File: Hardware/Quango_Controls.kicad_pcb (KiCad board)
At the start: 2 copper layers, 80.8 x 110 mm, 33 parts, among them J1 Conn_01x12_Male, J10 Gate_Out, J2 Conn_01x16_Male, J3 Conn_01x12_Male, J4 Conn_01x12_Male, J5 CV_A, J6 CV_B, J7 Out, J8 USB_C_Receptacle, J9 Midi_In, SW1 SW_Push, SW2 SW_Push

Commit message: Updates to Panel Graphics
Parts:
- moved J8 0.50 mm to (100.4, 124.2)
- moved J9 0.50 mm to (80.6, 124.3)
- moved R1 0.50 mm to (98.1, 124.2)
- moved R2 0.50 mm to (102.8, 124.2)
- moved TP1 0.50 mm to (91.5, 126.6)
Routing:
- net +3.3VA: track 259.7 -> 260.3 mm
- net /USB_DP: track 64.8 -> 64.2 mm

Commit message: Final Updates for v1.0 production
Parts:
- J1, J3, J4: footprint Connector_PinHeader_2.54mm:PinHeader_1x12_P2.54mm_Vertical -> Connector_PinSocket_2.54mm:PinSocket_1x12_P2.54mm_Vertical
- J2: footprint Connector_PinHeader_2.54mm:PinHeader_1x16_P2.54mm_Vertical -> Connector_PinSocket_2.54mm:PinSocket_1x16_P2.54mm_Vertical
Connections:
- J2 pad 13: /Gate3_Out -> /Gate4_Out
- J2 pad 14: /Gate4_Out -> /Gate3_Out
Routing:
- net /Gate3_Out: track 34.5 -> 31.6 mm
- net /MIDI_IN: track 100.3 -> 99.3 mm
- net +3.3VA: track 260.3 -> 259.6 mm
- net GND: vias 4 -> 84

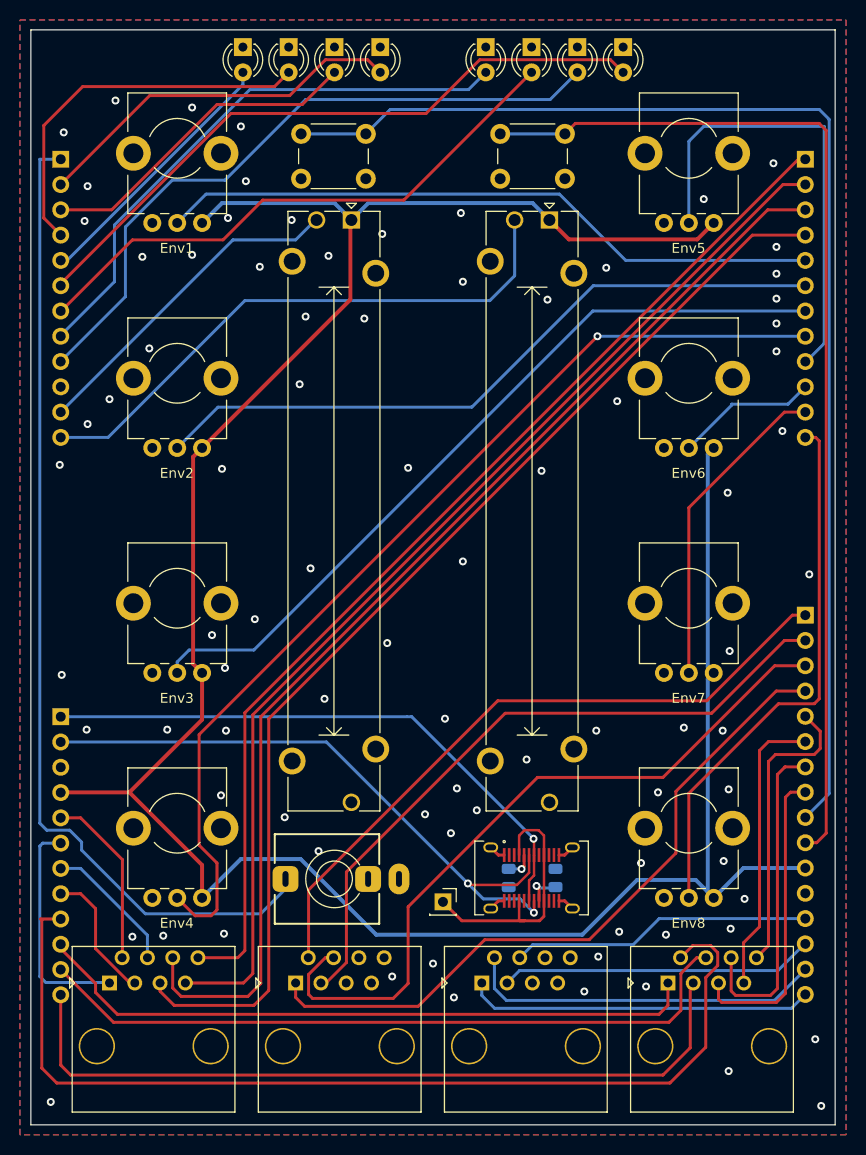
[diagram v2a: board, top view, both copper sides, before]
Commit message: Updated controls to include octave switching; revised panel
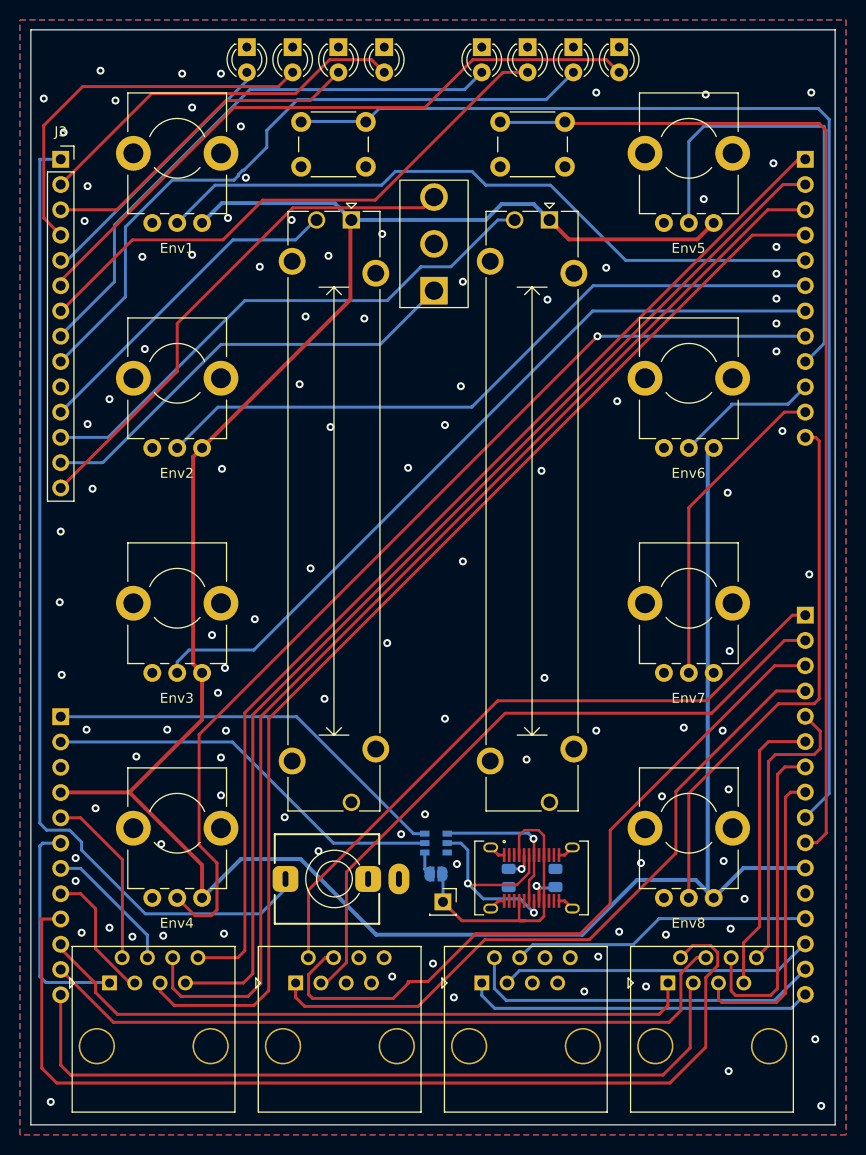
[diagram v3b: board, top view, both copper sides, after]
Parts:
- added JP1: Jumper, Jumper:SolderJumper-2_P1.3mm_Open_RoundedPad1.0x1.5mm, B.Cu at (90.8, 123.8)
- added SW3: Octave_Switch, Custom_Footprints:SP3T_Mini_Switch, F.Cu at (90.6, 60.5)
- added U1: STF202-22T1G, Custom_Footprints:STF202-22T1G, B.Cu at (90.8, 120.7)
- J3: value Conn_01x12_Male -> Conn_01x14_Male; footprint Connector_PinSocket_2.54mm:PinSocket_1x12_P2.54mm_Vertical -> Connector_PinSocket_2.54mm:PinSocket_1x14_P2.54mm_Vertical; moved to F.Cu
- moved SW1 1.20 mm to (80.5, 50.5)
- moved SW2 1.20 mm to (100.5, 50.5)
- moved A2 0.40 mm to (76.4, 42.0)
- moved A3 0.40 mm to (81.0, 42.0)
- moved B2 0.40 mm to (100.0, 42.0)
- moved B3 0.40 mm to (104.6, 42.0)
- moved A1 0.40 mm to (71.8, 42.0)
- moved A4 0.40 mm to (85.6, 42.0)
- moved B1 0.40 mm to (95.4, 42.0)
- moved B4 0.40 mm to (109.2, 42.0)
- turned J3 to 0 degrees
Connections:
- net Net-(J8-PadA4) renamed /VBUS
- J8 pad A6: /USB_DP -> /D+
- J8 pad A7: /USB_DM -> /D-
- J8 pad B6: /USB_DP -> /D+
- J8 pad B7: /USB_DM -> /D-
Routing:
- net /Octave_Down: track 0.00 -> 52.4 mm
- net /Octave_Up: track 0.00 -> 44.7 mm
- net /USB_DP: track 64.5 -> 40.8 mm, vias 2 -> 0
- net /D+: track 0.00 -> 23.4 mm, vias 0 -> 2
- net /USB_DM: track 59.0 -> 41.4 mm, vias 1 -> 0
- net /D-: track 0.00 -> 15.4 mm, vias 0 -> 1
- net /ChannelB_Level: track 57.9 -> 54.6 mm
- net /VBUS: track 26.6 -> 29.5 mm
- net Net-(JP1-Pad1): track 0.00 -> 2.35 mm
- net /Env1_Attack: track 67.1 -> 68.9 mm
- net /EnvB3_LED_Out: track 68.0 -> 68.7 mm
- net GND: vias 84 -> 104
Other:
- board text added: "Mountjoy Modular 2023 Quango Controls v2.0"
- board text removed: "Mountjoy Modular 2023 Quango Controls v1.0"

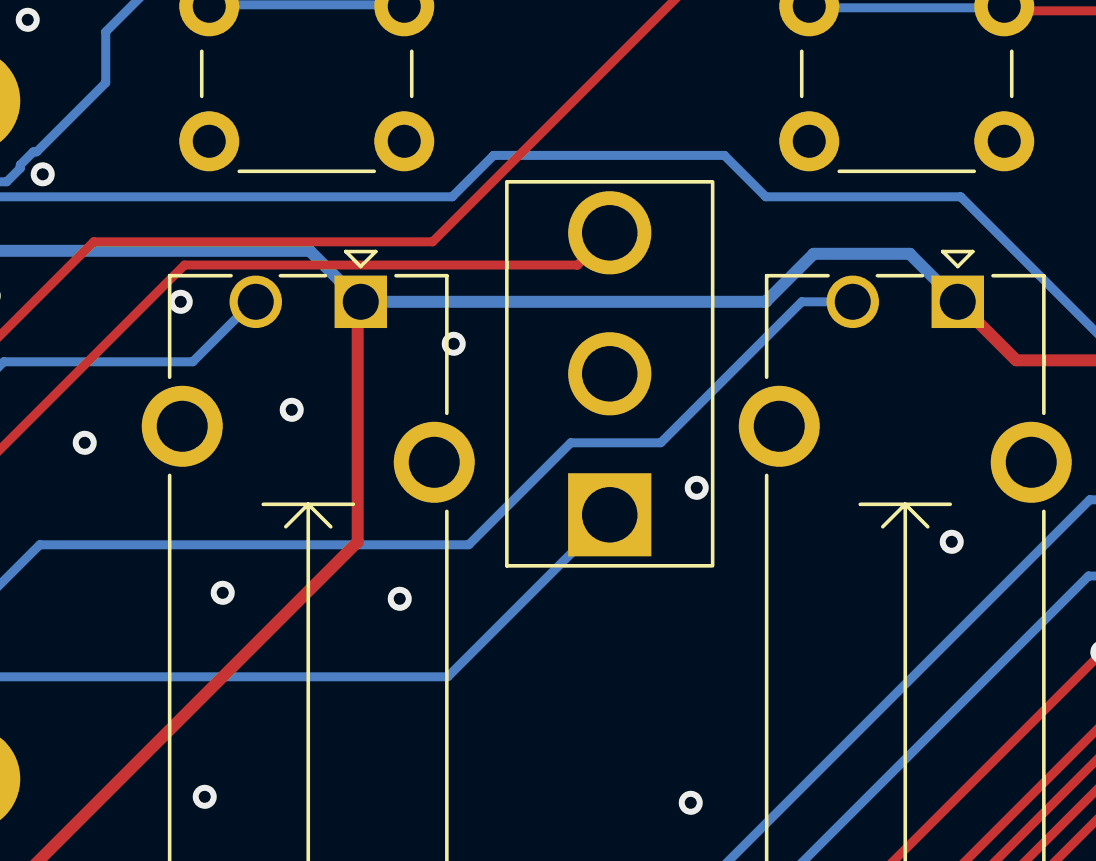
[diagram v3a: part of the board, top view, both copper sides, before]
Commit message: Prepared v2 controls and panel for  manufacture
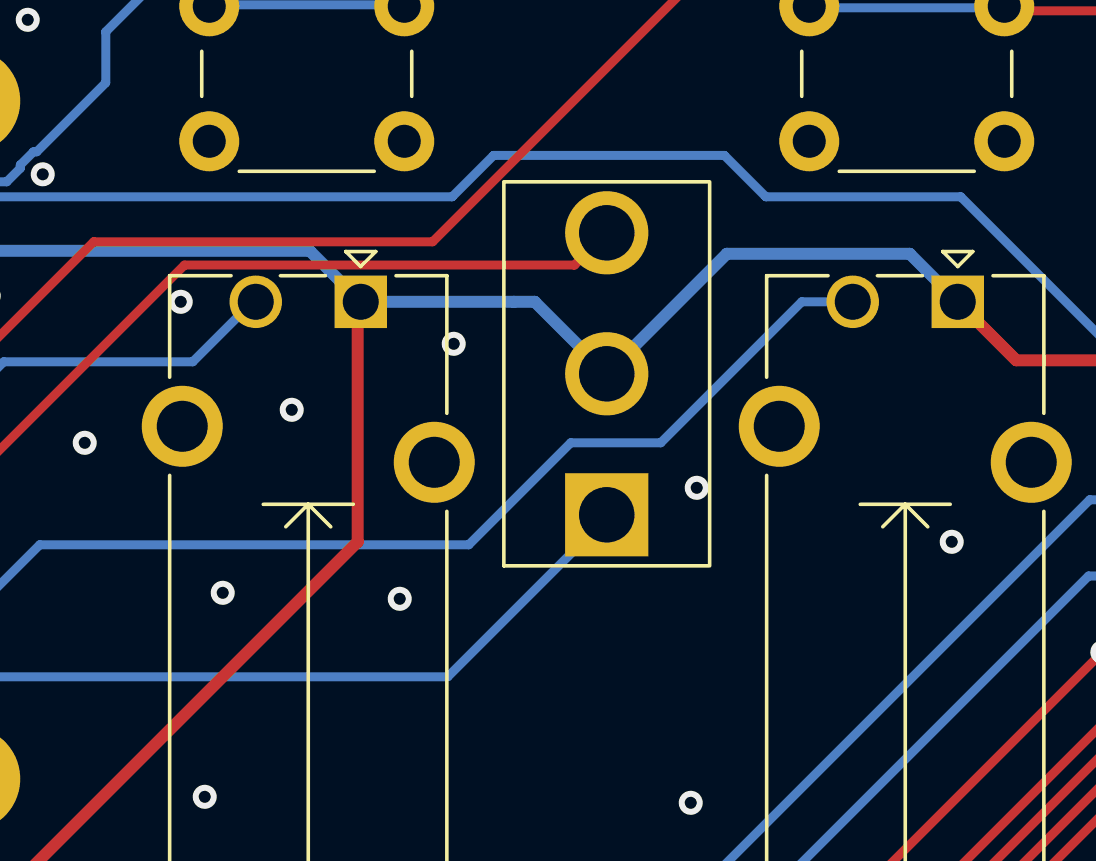
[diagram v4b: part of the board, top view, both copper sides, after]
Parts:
- moved SW3 0.10 mm to (90.5, 60.5)
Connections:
- SW3 pad 2: +3V3 -> +3.3VA
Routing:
- net +3.3VA: track 259.5 -> 261.5 mm
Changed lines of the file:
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@@
     (pad_to_mask_clearance 0)
     (pcbplotparams
-      (layerselection 0x00010fc_ffffffff)
+      (layerselection 0x00010f0_ffffffff)
       (disableapertmacros false)
       (usegerberextensions false)
@@
   (net 75 "/D-")
   (net 76 "Net-(JP1-Pad1)")
-  (net 77 "+3V3")
   (footprint "Custom_Footprints:LED_D3.0mm" (layer "F.Cu")
     (at 81 42 -90)
@@
   )
   (footprint "Custom_Footprints:SP3T_Mini_Switch" (layer "F.Cu")
-    (at 90.6 60.5 90)
+    (at 90.5 60.5 90)
     (property "Sheetfile" "Quango_Controls.kicad_sch")
     (property "Sheetname" "")
@@
       (net 52 "/Octave_Up") (pinfunction "1") (pintype "passive"))
     (pad "2" thru_hole circle (at 0 0 90) (size 2.775 2.775) (drill 1.85) (layers *.Cu *.Mask)
-      (net 77 "+3V3") (pinfunction "2") (pintype "passive"))
+      (net 10 "+3.3VA") (pinfunction "2") (pintype "passive"))
     (pad "3" thru_hole circle (at 4.7 0 90) (size 2.775 2.775) (drill 1.85) (layers *.Cu *.Mask)
       (net 72 "/Octave_Down") (pinfunction "3") (pintype "passive"))
@@
       (net 74 "/D+") (pinfunction "D1_IN") (pintype "bidirectional"))
     (pad "6" smd rect (at -0.95 1.125) (size 0.95 0.6) (layers "B.Cu" "B.Paste" "B.Mask")
-      (net 1 "GND") (pinfunction "GND") (pintype "bidirectional"))
+      (net 1 "GND") (pinfunction "GND") (pintype "power_in"))
   )
   (footprint "Connector_PinSocket_2.54mm:PinSocket_1x12_P2.54mm_Vertical" (layer "B.Cu")
@@
   (segment (start 80.6 56.4) (end 82.3 58.1) (width 0.4) (layer "B.Cu") (net 10))
   (segment (start 118.1 103) (end 118.7 103.6) (width 0.4) (layer "B.Cu") (net 10))
-  (segment (start 100.6 56.5) (end 102.2 58.1) (width 0.4) (layer "B.Cu") (net 10))
   (segment (start 105.5 129.9) (end 84.8 129.9) (width 0.4) (layer "B.Cu") (net 10))
-  (segment (start 95.8 58.1) (end 97.4 56.5) (width 0.4) (layer "B.Cu") (net 10))
   (segment (start 118.7 126.2) (end 121.7 123.2) (width 0.4) (layer "B.Cu") (net 10))
   (segment (start 84.8 129.9) (end 77.2 122.3) (width 0.4) (layer "B.Cu") (net 10))
-  (segment (start 97.4 56.5) (end 100.6 56.5) (width 0.4) (layer "B.Cu") (net 10))
   (segment (start 118.7 126.2) (end 116.9 124.4) (width 0.4) (layer "B.Cu") (net 10))
   (segment (start 118.7 81) (end 118.1 81.6) (width 0.4) (layer "B.Cu") (net 10))
@@
   (segment (start 118.1 125.6) (end 118.1 104.2) (width 0.4) (layer "B.Cu") (net 10))
   (segment (start 69.3 56.4) (end 80.6 56.4) (width 0.4) (layer "B.Cu") (net 10))
-  (segment (start 82.3 58.1) (end 95.8 58.1) (width 0.4) (layer "B.Cu") (net 10))
+  (segment (start 90.5 60.5) (end 94.5 56.5) (width 0.4) (layer "B.Cu") (net 10))
+  (segment (start 87.4 58.1) (end 88.1 58.1) (width 0.4) (layer "B.Cu") (net 10))
   (segment (start 67.3 58.4) (end 69.3 56.4) (width 0.4) (layer "B.Cu") (net 10))
   (segment (start 118.1 81.6) (end 118.1 103) (width 0.4) (layer "B.Cu") (net 10))
   (segment (start 118.1 104.2) (end 118.7 103.6) (width 0.4) (layer "B.Cu") (net 10))
+  (segment (start 94.5 56.5) (end 100.6 56.5) (width 0.4) (layer "B.Cu") (net 10))
   (segment (start 118.7 126.2) (end 118.1 125.6) (width 0.4) (layer "B.Cu") (net 10))
   (segment (start 71.2 122.3) (end 67.3 126.2) (width 0.4) (layer "B.Cu") (net 10))
+  (segment (start 88.1 58.1) (end 90.5 60.5) (width 0.4) (layer "B.Cu") (net 10))
   (segment (start 116.9 124.4) (end 111 124.4) (width 0.4) (layer "B.Cu") (net 10))
   (segment (start 121.7 123.2) (end 127.9 123.2) (width 0.4) (layer "B.Cu") (net 10))
   (segment (start 111 124.4) (end 105.5 129.9) (width 0.4) (layer "B.Cu") (net 10))
+  (segment (start 82.3 58.1) (end 87.4 58.1) (width 0.4) (layer "B.Cu") (net 10))
+  (segment (start 100.6 56.5) (end 102.2 58.1) (width 0.4) (layer "B.Cu") (net 10))
   (segment (start 109.86 62.16) (end 127.9 62.16) (width 0.3) (layer "B.Cu") (net 11))
   (segment (start 102.3 54.6) (end 109.86 62.16) (width 0.3) (layer "B.Cu") (net 11))
@@
   (segment (start 116.34 141.26) (end 116.34 134.75) (width 0.3) (layer "F.Cu") (net 45))
   (segment (start 53.1 135.94) (end 53.1 143) (width 0.3) (layer "F.Cu") (net 45))
+  (segment (start 90.5 65.3) (end 85.2 70.6) (width 0.3) (layer "B.Cu") (net 52))
+  (segment (start 90.5 65.2) (end 90.5 65.3) (width 0.3) (layer "B.Cu") (net 52))
+  (segment (start 85.2 70.6) (end 69.2 70.6) (width 0.3) (layer "B.Cu") (net 52))
+  (segment (start 57.32 82.48) (end 53.1 82.48) (width 0.3) (layer "B.Cu") (net 52))
   (segment (start 69.2 70.6) (end 57.32 82.48) (width 0.3) (layer "B.Cu") (net 52))
-  (segment (start 85.2 70.6) (end 69.2 70.6) (width 0.3) (layer "B.Cu") (net 52))
-  (segment (start 90.6 65.2) (end 85.2 70.6) (width 0.3) (layer "B.Cu") (net 52))
-  (segment (start 57.32 82.48) (end 53.1 82.48) (width 0.3) (layer "B.Cu") (net 52))
   (segment (start 99.65 123.05) (end 99.65 121.9) (width 0.3) (layer "F.Cu") (net 53))
   (segment (start 99.4 123.3) (end 99.65 123.05) (width 0.3) (layer "F.Cu") (net 53))
@@
   (segment (start 95.4 136) (end 96.7 137.3) (width 0.3) (layer "B.Cu") (net 67))
   (segment (start 126.5 137.3) (end 127.9 135.9) (width 0.3) (layer "B.Cu") (net 67))
-  (segment (start 90.6 55.8) (end 89.525 56.875) (width 0.3) (layer "F.Cu") (net 72))
-  (segment (start 89.525 56.875) (end 76.425 56.875) (width 0.3) (layer "F.Cu") (net 72))
-  (segment (start 64.8 73.32) (end 53.1 85.02) (width 0.3) (layer "F.Cu") (net 72))
   (segment (start 76.425 56.875) (end 64.8 68.5) (width 0.3) (layer "F.Cu") (net 72))
   (segment (start 64.8 68.5) (end 64.8 73.32) (width 0.3) (layer "F.Cu") (net 72))
+  (segment (start 64.8 73.32) (end 53.1 85.02) (width 0.3) (layer "F.Cu") (net 72))
+  (segment (start 90.5 55.8) (end 89.425 56.875) (width 0.3) (layer "F.Cu") (net 72))
+  (segment (start 89.425 56.875) (end 76.425 56.875) (width 0.3) (layer "F.Cu") (net 72))
   (segment (start 101.1 119.4) (end 101.65 119.95) (width 0.25) (layer "F.Cu") (net 73))
   (segment (start 99.2 128.5) (end 99.15 128.45) (width 0.3) (layer "F.Cu") (net 73))

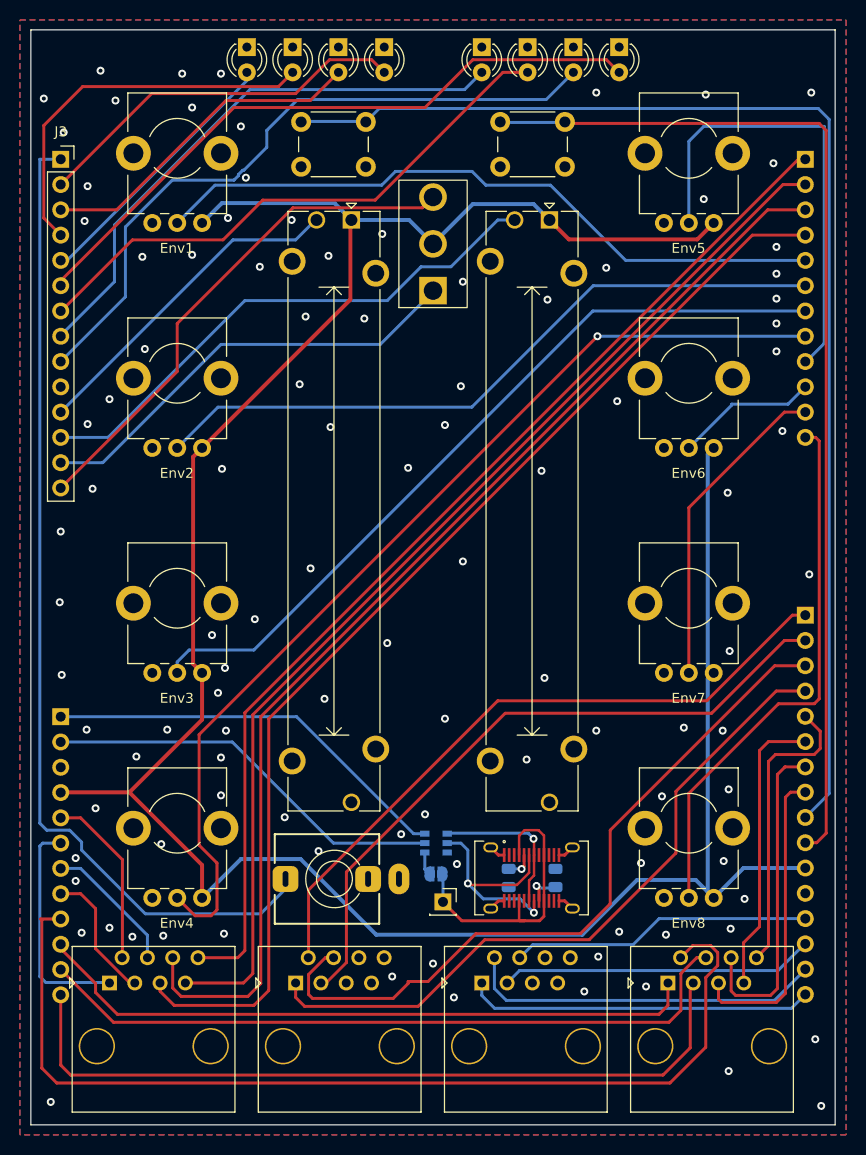
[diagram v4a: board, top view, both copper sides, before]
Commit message: Added header on control board for CV output
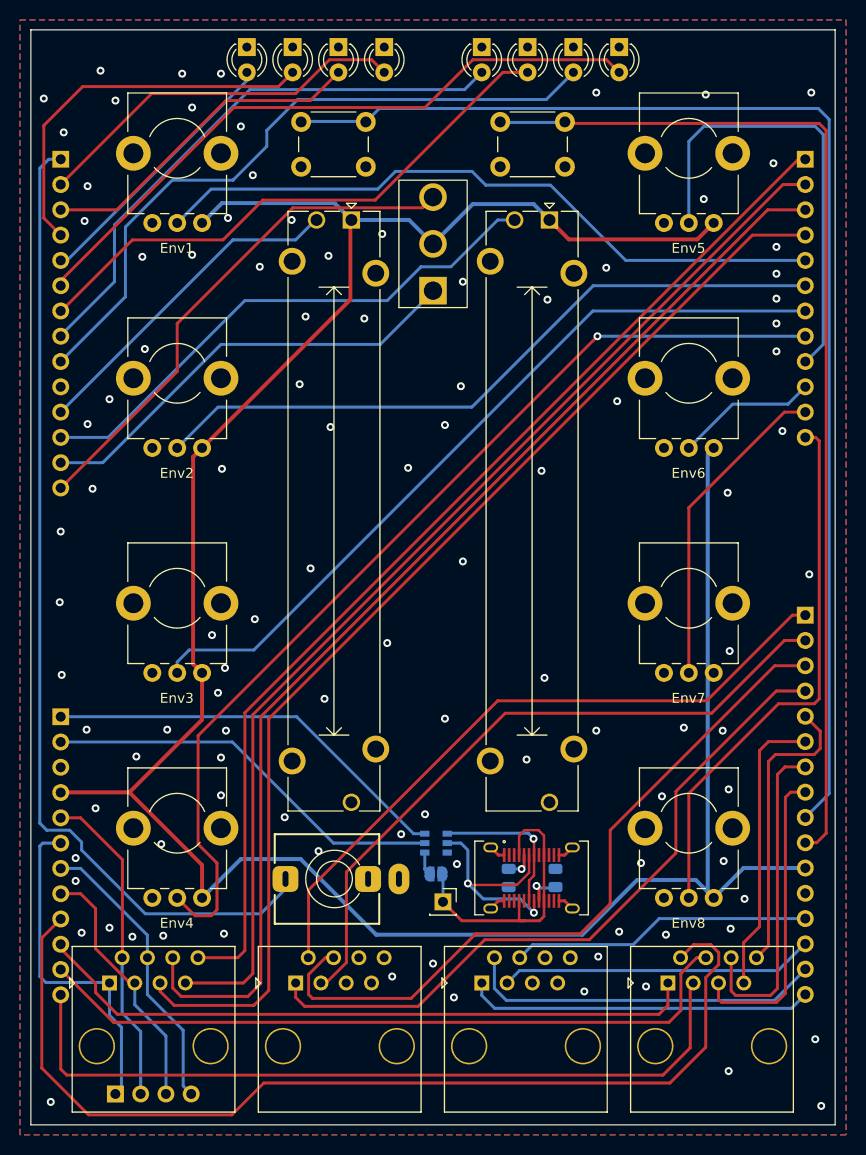
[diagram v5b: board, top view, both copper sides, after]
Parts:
- added J11: Conn_01x04_Male, Connector_PinHeader_2.54mm:PinHeader_1x04_P2.54mm_Vertical, B.Cu at (58.6, 145.9)
- J3: moved to B.Cu
- turned J3 to 180 degrees
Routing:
- net /CV_OUT_A4: track 13.7 -> 29.3 mm
- net /CV_OUT_A2: track 17.8 -> 32.3 mm
- net /CV_OUT_A3: track 13.5 -> 26.0 mm
- net /CV_OUT_A1: track 22.6 -> 34.5 mm
- net /CV_OUT_B2: track 100.4 -> 102.0 mm
- net /Env2_Attack: track 46.9 -> 46.3 mm
- net /MIDI_IN: track 99.3 -> 98.7 mm
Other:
- board text added: "1"
- board text added: "4"
- board text added: "CV Out A"
